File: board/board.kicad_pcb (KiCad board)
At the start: 4 copper layers, 24 x 29 mm, 5 parts, among them J1 020_1000BASE-T_with_CT, J2 004_BASE-T_CT, U1 MagJack-A70-112-331N126

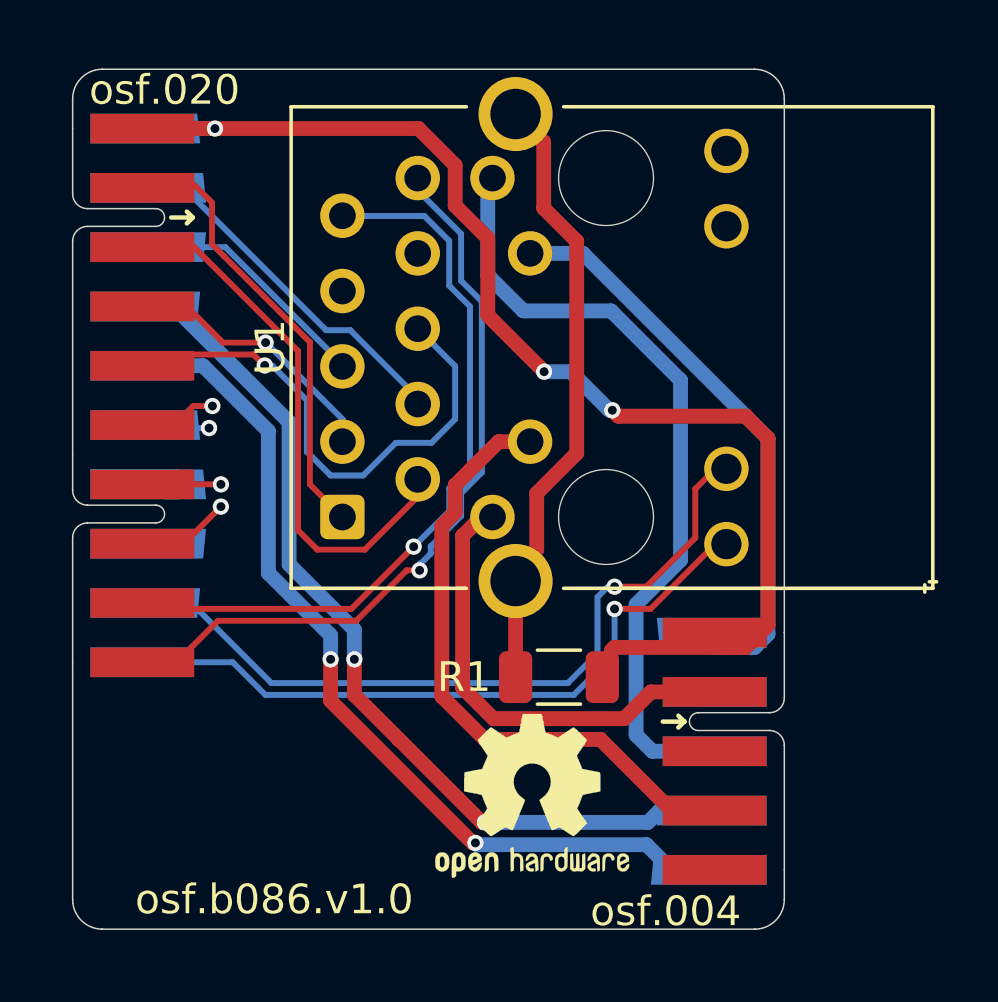
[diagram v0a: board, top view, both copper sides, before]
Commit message: led lines were backwards, fixed
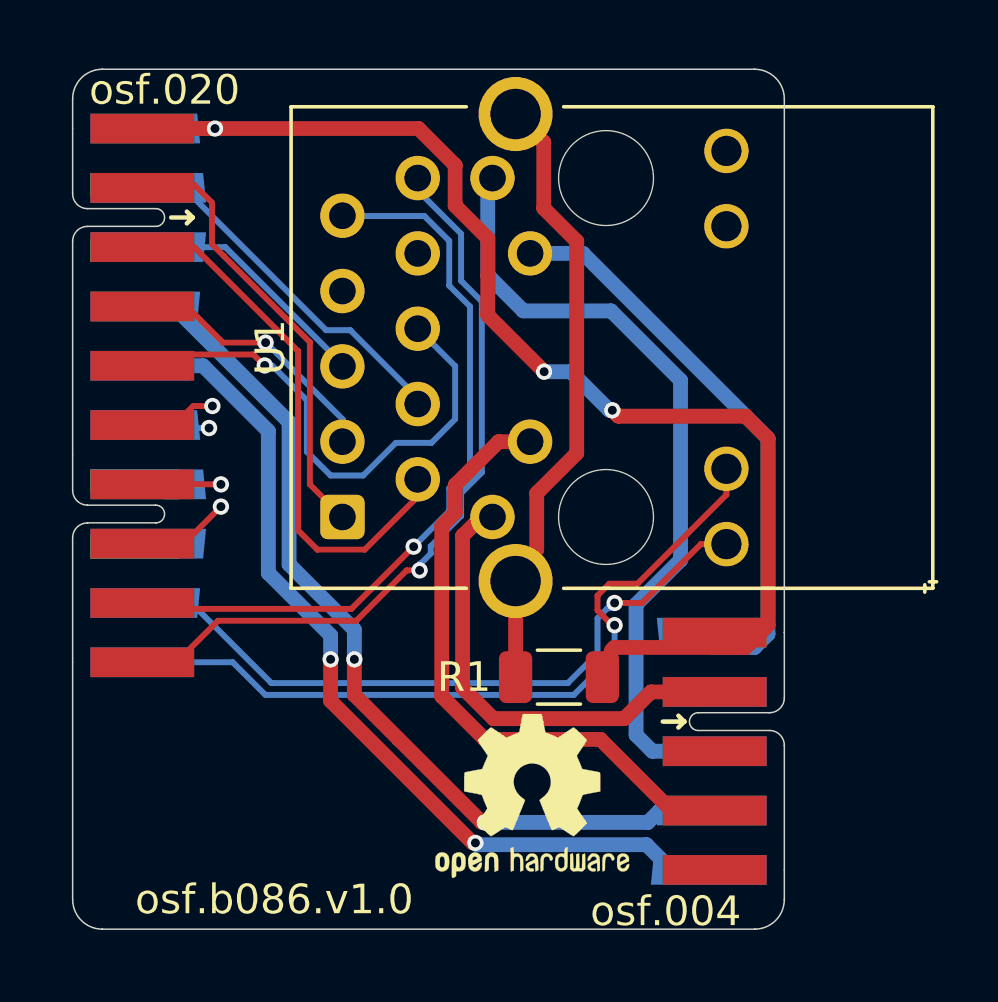
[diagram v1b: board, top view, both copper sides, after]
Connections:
- J1 pad 16: Net-(J1-Pad16) -> Net-(U1-Pad18)
- J1 pad 19: Net-(J1-Pad19) -> Net-(U1-Pad15)
- J1 pad 20: Net-(J1-Pad20) -> Net-(U1-Pad16)
- J1 pad 6: Net-(J1-Pad6) -> Net-(U1-Pad17)
- U1 pad 15: Net-(J1-Pad20) -> Net-(U1-Pad15)
- U1 pad 16: Net-(J1-Pad19) -> Net-(U1-Pad16)
- U1 pad 17: Net-(J1-Pad16) -> Net-(U1-Pad17)
- U1 pad 18: Net-(J1-Pad6) -> Net-(U1-Pad18)
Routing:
- net Net-(U1-Pad18): track 0.00 -> 27.2 mm, vias 0 -> 1
- net Net-(J1-Pad19): track 26.0 -> 0.00 mm, vias 1 -> 0
- net Net-(U1-Pad16): track 0.00 -> 25.9 mm, vias 0 -> 1
- net Net-(J1-Pad6): track 23.9 -> 0.00 mm, vias 1 -> 0
- net Net-(U1-Pad15): track 0.00 -> 23.4 mm, vias 0 -> 1
- net Net-(J1-Pad20): track 23.4 -> 0.00 mm, vias 1 -> 0
- net Net-(U1-Pad17): track 0.00 -> 23.3 mm, vias 0 -> 1
- net Net-(J1-Pad16): track 22.7 -> 0.00 mm, vias 1 -> 0
